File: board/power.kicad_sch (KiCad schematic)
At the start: 14 parts, among them IC1 HUSB238, J1 USB_C_Receptacle_USB2.0_14P, Q1 IRLML6402TRPBF

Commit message: The microcontroller
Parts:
- C1, C2, C3: footprint (none) -> Capacitor_SMD:C_0805_2012Metric
- D1, D2: footprint (none) -> LED_SMD:LED_0805_2012Metric
- IC1: footprint SON50P300X300X80-11N-D -> HUSB238:SON50P300X300X80-11N-D
- R1, R2, R3, R4, R5: footprint (none) -> Resistor_SMD:R_0805_2012Metric
- U1: value ~ -> SE5120; footprint (none) -> Package_TO_SOT_SMD:SOT-223
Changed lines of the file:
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@@
 			)
 		)
-		(property "Footprint" ""
+		(property "Footprint" "LED_SMD:LED_0805_2012Metric"
 			(at 26.67 132.08 0)
 			(effects
@@
 			)
 		)
-		(property "Footprint" ""
+		(property "Footprint" "Capacitor_SMD:C_0805_2012Metric"
 			(at 23.8252 96.52 0)
 			(effects
@@
 			)
 		)
-		(property "Footprint" ""
+		(property "Footprint" "Resistor_SMD:R_0805_2012Metric"
 			(at 90.932 35.56 90)
 			(effects
@@
 			)
 		)
-		(property "Footprint" "SON50P300X300X80-11N-D"
+		(property "Footprint" "HUSB238:SON50P300X300X80-11N-D"
 			(at 88.9 36.83 0)
 			(effects
@@
 			)
 		)
-		(property "Footprint" ""
+		(property "Footprint" "LED_SMD:LED_0805_2012Metric"
 			(at 16.51 132.08 0)
 			(effects
@@
 			)
 		)
-		(property "Footprint" ""
+		(property "Footprint" "Resistor_SMD:R_0805_2012Metric"
 			(at 24.892 124.46 90)
 			(effects
@@
 			)
 		)
-		(property "Footprint" ""
+		(property "Footprint" "Capacitor_SMD:C_0805_2012Metric"
 			(at 63.1952 38.1 0)
 			(effects
@@
 			)
 		)
-		(property "Footprint" ""
+		(property "Footprint" "Resistor_SMD:R_0805_2012Metric"
 			(at 101.092 45.72 90)
 			(effects
@@
 			)
 		)
-		(property "Footprint" ""
+		(property "Footprint" "Resistor_SMD:R_0805_2012Metric"
 			(at 14.732 124.46 90)
 			(effects
@@
 			)
 		)
-		(property "Value" "~"
+		(property "Value" "SE5120"
 			(at 38.735 83.82 0)
 			(effects
@@
 			)
 		)
-		(property "Footprint" ""
+		(property "Footprint" "Package_TO_SOT_SMD:SOT-223"
 			(at 38.1 86.36 0)
 			(effects
@@
 			)
 		)
-		(property "Footprint" ""
+		(property "Footprint" "Resistor_SMD:R_0805_2012Metric"
 			(at 82.042 27.94 90)
 			(effects
@@
 			)
 		)
-		(property "Footprint" ""
+		(property "Footprint" "Capacitor_SMD:C_0805_2012Metric"
 			(at 53.0352 96.52 0)
 			(effects

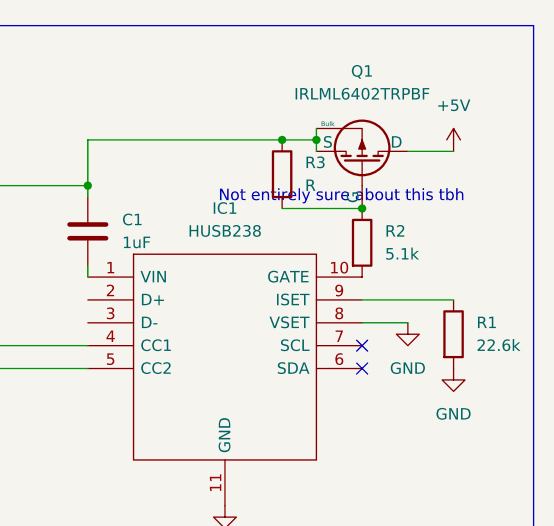
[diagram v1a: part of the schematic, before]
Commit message: Display Schematic
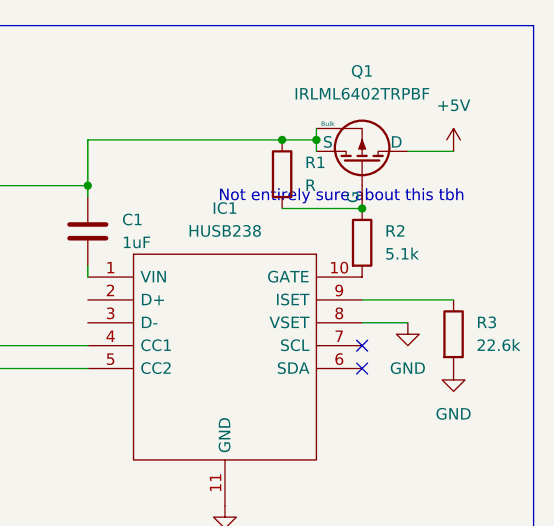
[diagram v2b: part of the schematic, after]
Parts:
- renumbered R3 to R1, R1 to R3
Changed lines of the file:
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@@
 		(dnp no)
 		(fields_autoplaced yes)
-		(property "Reference" "#PWR02"
+		(property "Reference" "#PWR04"
 			(at 77.47 71.12 0)
 			(effects
@@
 			(project "board"
 				(path "/380d0889-29f1-4d98-b1bb-ce6ede3c8d67/bd274052-b536-4fa6-b064-0da137bd167d"
-					(reference "#PWR02")
+					(reference "#PWR04")
 					(unit 1)
 				)
@@
 		(dnp no)
 		(fields_autoplaced yes)
-		(property "Reference" "#PWR03"
+		(property "Reference" "#PWR02"
 			(at 97.79 50.8 0)
 			(effects
@@
 			(project ""
 				(path "/380d0889-29f1-4d98-b1bb-ce6ede3c8d67/bd274052-b536-4fa6-b064-0da137bd167d"
-					(reference "#PWR03")
+					(reference "#PWR02")
 					(unit 1)
 				)
@@
 		(dnp no)
 		(fields_autoplaced yes)
-		(property "Reference" "#PWR01"
+		(property "Reference" "#PWR05"
 			(at 27.94 73.66 0)
 			(effects
@@
 			(project ""
 				(path "/380d0889-29f1-4d98-b1bb-ce6ede3c8d67/bd274052-b536-4fa6-b064-0da137bd167d"
-					(reference "#PWR01")
+					(reference "#PWR05")
 					(unit 1)
 				)
@@
 		(dnp no)
 		(fields_autoplaced yes)
-		(property "Reference" "#PWR07"
+		(property "Reference" "#PWR06"
 			(at 22.86 92.71 0)
 			(effects
@@
 			(project "board"
 				(path "/380d0889-29f1-4d98-b1bb-ce6ede3c8d67/bd274052-b536-4fa6-b064-0da137bd167d"
-					(reference "#PWR07")
+					(reference "#PWR06")
 					(unit 1)
 				)
@@
 		(dnp no)
 		(fields_autoplaced yes)
-		(property "Reference" "#PWR08"
+		(property "Reference" "#PWR07"
 			(at 52.07 92.71 0)
 			(effects
@@
 			(project ""
 				(path "/380d0889-29f1-4d98-b1bb-ce6ede3c8d67/bd274052-b536-4fa6-b064-0da137bd167d"
-					(reference "#PWR08")
+					(reference "#PWR07")
 					(unit 1)
 				)
@@
 		(dnp no)
 		(fields_autoplaced yes)
-		(property "Reference" "#PWR011"
+		(property "Reference" "#PWR09"
 			(at 16.51 124.46 0)
 			(effects
@@
 			(project ""
 				(path "/380d0889-29f1-4d98-b1bb-ce6ede3c8d67/bd274052-b536-4fa6-b064-0da137bd167d"
-					(reference "#PWR011")
+					(reference "#PWR09")
 					(unit 1)
 				)
@@
 		(dnp no)
 		(fields_autoplaced yes)
-		(property "Reference" "#PWR06"
+		(property "Reference" "#PWR08"
 			(at 43.18 104.14 0)
 			(effects
@@
 			(project ""
 				(path "/380d0889-29f1-4d98-b1bb-ce6ede3c8d67/bd274052-b536-4fa6-b064-0da137bd167d"
-					(reference "#PWR06")
+					(reference "#PWR08")
 					(unit 1)
 				)
@@
 		(dnp no)
 		(fields_autoplaced yes)
-		(property "Reference" "#PWR04"
+		(property "Reference" "#PWR03"
 			(at 102.87 55.88 0)
 			(effects
@@
 			(project "board"
 				(path "/380d0889-29f1-4d98-b1bb-ce6ede3c8d67/bd274052-b536-4fa6-b064-0da137bd167d"
-					(reference "#PWR04")
+					(reference "#PWR03")
 					(unit 1)
 				)
@@
 		(dnp no)
 		(fields_autoplaced yes)
-		(property "Reference" "R1"
+		(property "Reference" "R3"
 			(at 105.41 44.4499 0)
 			(effects
@@
 			(project ""
 				(path "/380d0889-29f1-4d98-b1bb-ce6ede3c8d67/bd274052-b536-4fa6-b064-0da137bd167d"
-					(reference "R1")
+					(reference "R3")
 					(unit 1)
 				)
@@
 		(dnp no)
 		(fields_autoplaced yes)
-		(property "Reference" "#PWR09"
+		(property "Reference" "#PWR011"
 			(at 21.59 144.78 0)
 			(effects
@@
 			(project ""
 				(path "/380d0889-29f1-4d98-b1bb-ce6ede3c8d67/bd274052-b536-4fa6-b064-0da137bd167d"
-					(reference "#PWR09")
+					(reference "#PWR011")
 					(unit 1)
 				)
@@
 		(dnp no)
 		(fields_autoplaced yes)
-		(property "Reference" "R3"
+		(property "Reference" "R1"
 			(at 86.36 26.6699 0)
 			(effects
@@
 			(project ""
 				(path "/380d0889-29f1-4d98-b1bb-ce6ede3c8d67/bd274052-b536-4fa6-b064-0da137bd167d"
-					(reference "R3")
+					(reference "R1")
 					(unit 1)
 				)
@@
 		(dnp no)
 		(fields_autoplaced yes)
-		(property "Reference" "#PWR05"
+		(property "Reference" "#PWR01"
 			(at 102.87 29.21 0)
 			(effects
@@
 			(project ""
 				(path "/380d0889-29f1-4d98-b1bb-ce6ede3c8d67/bd274052-b536-4fa6-b064-0da137bd167d"
-					(reference "#PWR05")
-					(unit 1)
-				)
+					(reference "#PWR01")
+					(unit 1)
+				)

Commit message: Lots of silly train things
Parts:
- removed U1: SE5120, Package_TO_SOT_SMD:SOT-223, symbol TrainLocsBoard:SE5120
- added U1: SED5120, LCSC:SOT-223-3_L6.5-W3.4-P2.30-LS7.0-BR, symbol LCSC:SED5120
- J1: footprint (none) -> Connector_USB:USB_C_Receptacle_G-Switch_GT-USB-7010ASV
- Q1: footprint (none) -> LCSC:SOT-23-3_L2.9-W1.6-P1.90-LS2.8-BR
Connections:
- net +3V3: now also U1.3 (VOUT)
- net +5V: now also U1.1 (VIN)
- net GND: now also U1.2 (GND), U1.4 (TAB)
- net at J1.A6 (D+): now also IC1.2 (D+), J1.B6 (D+)
- net at J1.A7 (D-): now also IC1.3 (D-), J1.B7 (D-)
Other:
- moved on the sheet: C2, C3
